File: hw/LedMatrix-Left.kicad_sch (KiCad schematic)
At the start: 76 parts, among them Q3200 DTA114E, Q3201 DTA114E, Q3202 DTA114E, Q3203 DTA114E, Q3204 DTA114E, Q3205 DTA114E, Q3206 DTA114E, Q3207 DTA114E, Q3208 DTA114E, Q3209 DTA114E, Q3210 DTC114EE, Q3211 DTC114EE, Q3212 DTC114EE, Q3213 DTC114EE, Q3214 DTC114EE, Q3215 DTC114EE, Q3216 DTC114EE, Q3217 DTC114EE, Q3218 DTC114EE, Q3219 DTC114EE, Q3220 DTC114EE, Q3221 DTC114EE, X3200 Lightpipe-5x5mm-Dome, X3201 Lightpipe-5x5mm-Dome

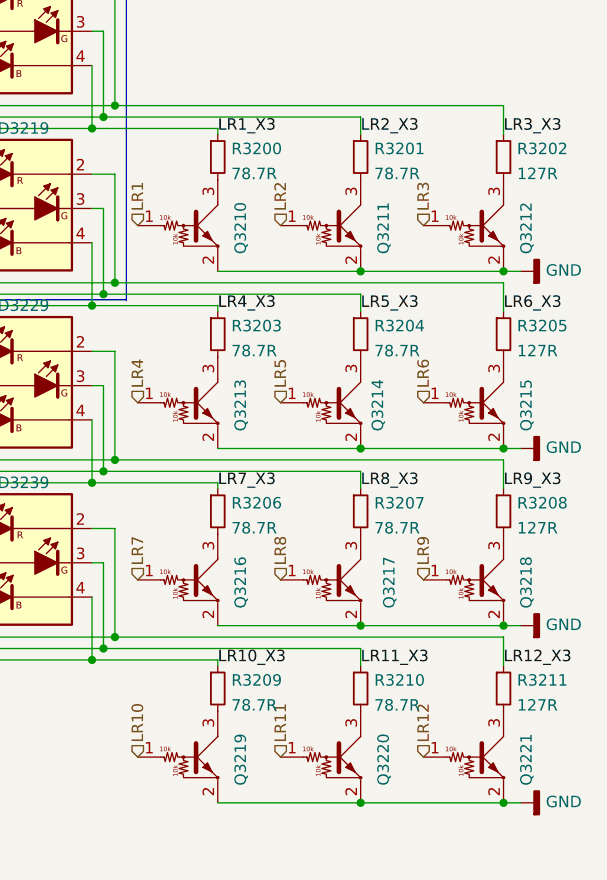
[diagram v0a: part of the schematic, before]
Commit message: Add 300R symbol and use it at green LEDs.
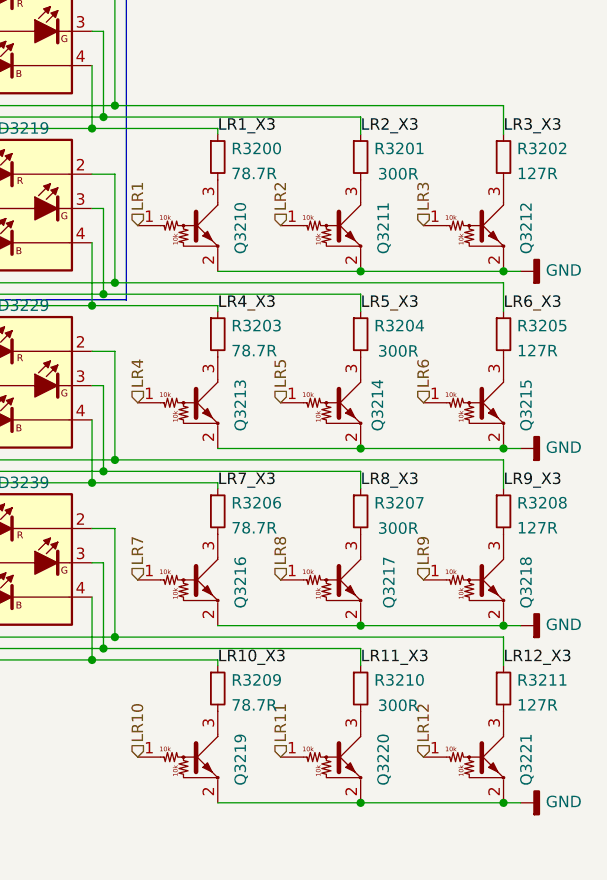
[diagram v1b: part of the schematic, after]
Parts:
- R3201, R3204, R3207, R3210: value 78.7R -> 300R; symbol Keyboard:78.7R -> Keyboard:300R; manf# RC0402FR-0778R7L -> ERJ-2RKF3000X; mouser# 603-RC0402FR-0778R7L -> 667-ERJ-2RKF3000X
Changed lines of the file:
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@@
     (pin "2")
   )
-  (symbol (lib_id "Keyboard:78.7R") (at 257.81 117.475 0) (unit 1)
-    (in_bom yes) (on_board yes) (fields_autoplaced)
+  (symbol (lib_id "Keyboard:300R") (at 257.81 117.475 0) (unit 1)
+    (in_bom yes) (on_board yes)
     (property "Reference" "R3210" (id 0) (at 259.3086 116.5665 0)
       (effects (font (size 1.27 1.27)) (justify left))
     )
-    (property "Value" "78.7R" (id 1) (at 259.3086 119.3416 0)
+    (property "Value" "300R" (id 1) (at 259.715 119.38 0)
       (effects (font (size 1.27 1.27)) (justify left))
     )
@@
       (effects (font (size 1.27 1.27)) hide)
     )
-    (property "Datasheet" "https://www.mouser.de/datasheet/2/447/PYu_RC_Group_51_RoHS_L_10-1664068.pdf" (id 3) (at 258.572 116.967 0)
-      (effects (font (size 1.27 1.27)) hide)
-    )
-    (property "mouser#" "603-RC0402FR-0778R7L" (id 4) (at 261.112 114.427 0)
-      (effects (font (size 1.524 1.524)) hide)
-    )
-    (property "manf#" "RC0402FR-0778R7L" (id 5) (at 257.81 117.475 0)
+    (property "Datasheet" "https://www.mouser.de/datasheet/2/315/AOA0000C304-1149620.pdf" (id 3) (at 258.572 116.967 0)
+      (effects (font (size 1.27 1.27)) hide)
+    )
+    (property "mouser#" "667-ERJ-2RKF3000X" (id 4) (at 261.112 114.427 0)
+      (effects (font (size 1.524 1.524)) hide)
+    )
+    (property "manf#" "ERJ-2RKF3000X " (id 5) (at 257.81 117.475 0)
       (effects (font (size 1.27 1.27)) hide)
     )
@@
     (pin "2")
   )
-  (symbol (lib_id "Keyboard:78.7R") (at 257.81 78.105 0) (unit 1)
-    (in_bom yes) (on_board yes) (fields_autoplaced)
+  (symbol (lib_id "Keyboard:300R") (at 257.81 78.105 0) (unit 1)
+    (in_bom yes) (on_board yes)
     (property "Reference" "R3204" (id 0) (at 259.3086 77.1965 0)
       (effects (font (size 1.27 1.27)) (justify left))
     )
-    (property "Value" "78.7R" (id 1) (at 259.3086 79.9716 0)
+    (property "Value" "300R" (id 1) (at 259.715 80.01 0)
       (effects (font (size 1.27 1.27)) (justify left))
     )
@@
       (effects (font (size 1.27 1.27)) hide)
     )
-    (property "Datasheet" "https://www.mouser.de/datasheet/2/447/PYu_RC_Group_51_RoHS_L_10-1664068.pdf" (id 3) (at 258.572 77.597 0)
-      (effects (font (size 1.27 1.27)) hide)
-    )
-    (property "mouser#" "603-RC0402FR-0778R7L" (id 4) (at 261.112 75.057 0)
-      (effects (font (size 1.524 1.524)) hide)
-    )
-    (property "manf#" "RC0402FR-0778R7L" (id 5) (at 257.81 78.105 0)
+    (property "Datasheet" "https://www.mouser.de/datasheet/2/315/AOA0000C304-1149620.pdf" (id 3) (at 258.572 77.597 0)
+      (effects (font (size 1.27 1.27)) hide)
+    )
+    (property "mouser#" "667-ERJ-2RKF3000X" (id 4) (at 261.112 75.057 0)
+      (effects (font (size 1.524 1.524)) hide)
+    )
+    (property "manf#" "ERJ-2RKF3000X " (id 5) (at 257.81 78.105 0)
       (effects (font (size 1.27 1.27)) hide)
     )
@@
     (pin "2")
   )
-  (symbol (lib_id "Keyboard:78.7R") (at 257.81 97.79 0) (unit 1)
-    (in_bom yes) (on_board yes) (fields_autoplaced)
+  (symbol (lib_id "Keyboard:300R") (at 257.81 97.79 0) (unit 1)
+    (in_bom yes) (on_board yes)
     (property "Reference" "R3207" (id 0) (at 259.3086 96.8815 0)
       (effects (font (size 1.27 1.27)) (justify left))
     )
-    (property "Value" "78.7R" (id 1) (at 259.3086 99.6566 0)
+    (property "Value" "300R" (id 1) (at 259.715 99.695 0)
       (effects (font (size 1.27 1.27)) (justify left))
     )
@@
       (effects (font (size 1.27 1.27)) hide)
     )
-    (property "Datasheet" "https://www.mouser.de/datasheet/2/447/PYu_RC_Group_51_RoHS_L_10-1664068.pdf" (id 3) (at 258.572 97.282 0)
-      (effects (font (size 1.27 1.27)) hide)
-    )
-    (property "mouser#" "603-RC0402FR-0778R7L" (id 4) (at 261.112 94.742 0)
-      (effects (font (size 1.524 1.524)) hide)
-    )
-    (property "manf#" "RC0402FR-0778R7L" (id 5) (at 257.81 97.79 0)
+    (property "Datasheet" "https://www.mouser.de/datasheet/2/315/AOA0000C304-1149620.pdf" (id 3) (at 258.572 97.282 0)
+      (effects (font (size 1.27 1.27)) hide)
+    )
+    (property "mouser#" "667-ERJ-2RKF3000X" (id 4) (at 261.112 94.742 0)
+      (effects (font (size 1.524 1.524)) hide)
+    )
+    (property "manf#" "ERJ-2RKF3000X " (id 5) (at 257.81 97.79 0)
       (effects (font (size 1.27 1.27)) hide)
     )
@@
     (pin "2")
   )
-  (symbol (lib_id "Keyboard:78.7R") (at 257.81 58.42 0) (unit 1)
-    (in_bom yes) (on_board yes) (fields_autoplaced)
+  (symbol (lib_id "Keyboard:300R") (at 257.81 58.42 0) (unit 1)
+    (in_bom yes) (on_board yes)
     (property "Reference" "R3201" (id 0) (at 259.3086 57.5115 0)
       (effects (font (size 1.27 1.27)) (justify left))
     )
-    (property "Value" "78.7R" (id 1) (at 259.3086 60.2866 0)
+    (property "Value" "300R" (id 1) (at 259.715 60.325 0)
       (effects (font (size 1.27 1.27)) (justify left))
     )
@@
       (effects (font (size 1.27 1.27)) hide)
     )
-    (property "Datasheet" "https://www.mouser.de/datasheet/2/447/PYu_RC_Group_51_RoHS_L_10-1664068.pdf" (id 3) (at 258.572 57.912 0)
-      (effects (font (size 1.27 1.27)) hide)
-    )
-    (property "mouser#" "603-RC0402FR-0778R7L" (id 4) (at 261.112 55.372 0)
-      (effects (font (size 1.524 1.524)) hide)
-    )
-    (property "manf#" "RC0402FR-0778R7L" (id 5) (at 257.81 58.42 0)
-      (effects (font (size 1.27 1.27)) hide)
-    )
+    (property "Datasheet" "https://www.mouser.de/datasheet/2/315/AOA0000C304-1149620.pdf" (id 3) (at 258.572 57.912 0)
+      (effects (font (size 1.27 1.27)) hide)
+    )
+    (property "mouser#" "667-ERJ-2RKF3000X" (id 4) (at 261.112 55.372 0)
+      (effects (font (size 1.524 1.524)) hide)
+    )
+    (property "manf#" "ERJ-2RKF3000X " (id 5) (at 257.81 58.42 0)
+      (effects (font (size 1.27 1.27)) hide)
+    )
